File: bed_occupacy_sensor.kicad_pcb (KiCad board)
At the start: 2 copper layers, 10 parts, among them J1 FSR_2, J2 FSR_1, U1 mini_esp32

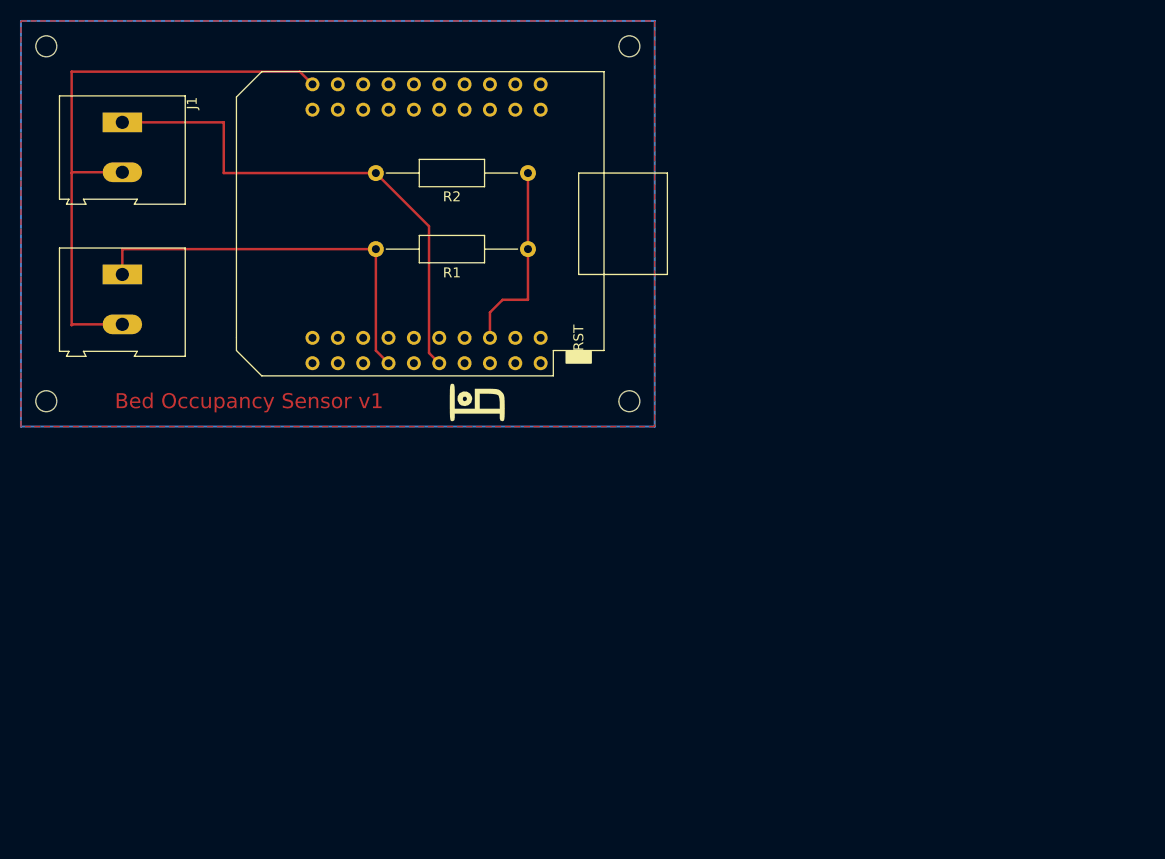
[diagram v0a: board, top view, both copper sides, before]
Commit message: new pcb design all GND connected to ground plane
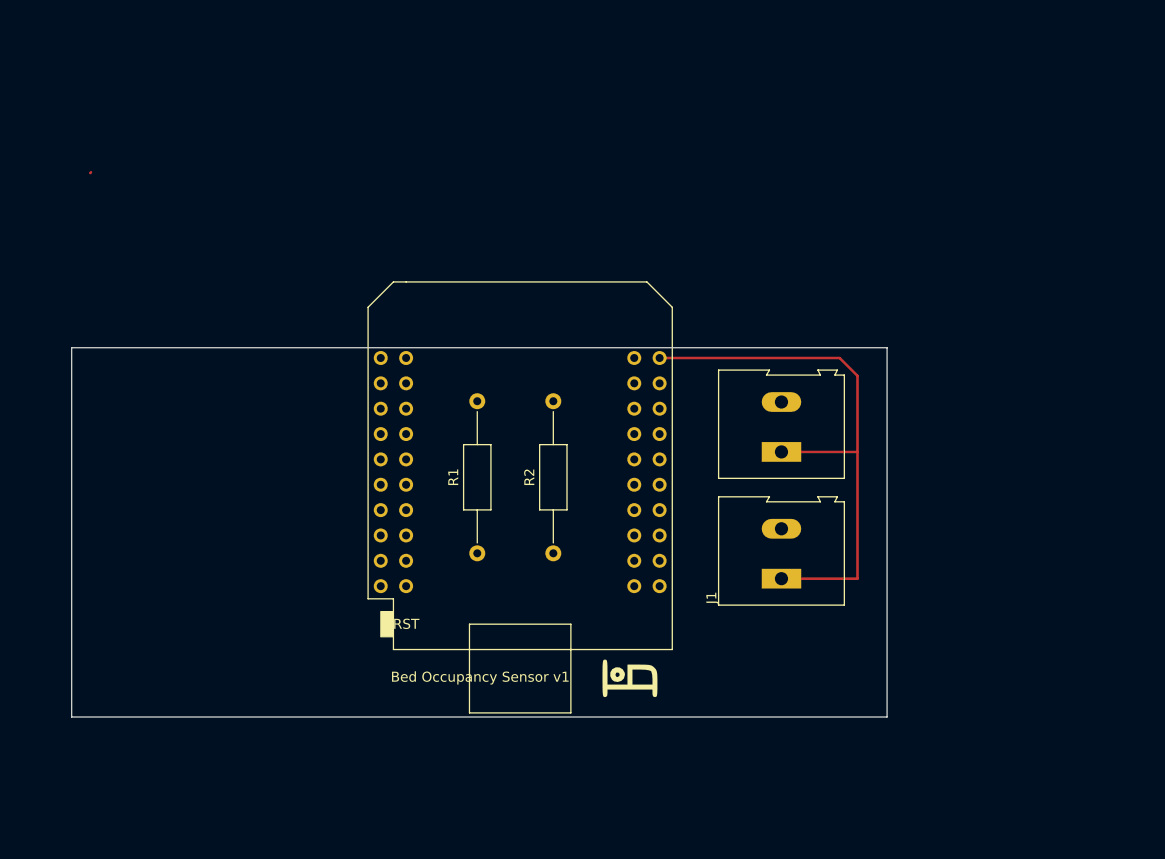
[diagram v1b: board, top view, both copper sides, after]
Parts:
- removed REF** (x4): MountingHole_2.1mm, MountingHole:MountingHole_2.1mm
- moved J1 80.3 mm to (170.2, 104.1), turned to 90 degrees
- moved J2 68.4 mm to (170.2, 91.4), turned to 90 degrees
- moved R2 38.2 mm to (147.3, 101.6), turned to 90 degrees
- moved G*** 31.6 mm to (155.0, 114.0)
- moved R1 30.9 mm to (139.7, 101.6), turned to 90 degrees
- moved U1 26.6 mm to (144.0, 93.5), turned to 0 degrees
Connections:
- J1 pad 1: Net-(J1-Pad1) -> Net-(U1-Pad22)
- J1 pad 2: Net-(U1-Pad22) -> Net-(R1-Pad2)
- J2 pad 1: Net-(J2-Pad1) -> Net-(U1-Pad22)
- J2 pad 2: Net-(U1-Pad22) -> Net-(R2-Pad2)
- R1 pad 2: Net-(J2-Pad1) -> Net-(R1-Pad2)
- R2 pad 2: Net-(J1-Pad1) -> Net-(R2-Pad2)
- U1 pad 11: Net-(J1-Pad1) -> Net-(R2-Pad2)
- U1 pad 7: Net-(J2-Pad1) -> Net-(R1-Pad2)
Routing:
- net Net-(J1-Pad1): track 52.2 -> 0.00 mm
- net Net-(J2-Pad1): track 39.9 -> 0.00 mm
- net Net-(R1-Pad1): track 19.6 -> 0.00 mm
- net Net-(U1-Pad22): track 60.3 -> 56.1 mm
- removed copper zone on F.Cu, net (none)
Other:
- board outline added: 81.7 x 37 mm

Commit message: Save-Changes again
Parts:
- moved R1 46.9 mm to (185.0, 113.6)
- moved R2 46.9 mm to (192.6, 113.6)
- moved U1 46.9 mm to (189.3, 105.5)
- moved G*** 26.0 mm to (165.0, 90.0)
- moved J2 20.4 mm to (164.7, 111.1), turned to -90 degrees
- moved J1 7.96 mm to (164.7, 98.4), turned to -90 degrees
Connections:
- net Net-(R1-Pad1) renamed /+3V3
- net Net-(R1-Pad2) renamed /SIDE_A
- net Net-(R2-Pad2) renamed /SIDE_B
- J1 pad 1: Net-(U1-Pad22) -> /GND
- J2 pad 1: Net-(U1-Pad22) -> /GND
- U1 pad 1: unconnected-(U1-Pad1) -> /GND
- U1 pad 22: Net-(U1-Pad22) -> /GND
- U1 pad 33: unconnected-(U1-Pad33) -> /GND
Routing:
- net /SIDE_B: track 0.00 -> 74.8 mm
- net Net-(U1-Pad22): track 56.1 -> 0.00 mm
- net /SIDE_A: track 0.00 -> 22.4 mm
- net /+3V3: track 0.00 -> 15.5 mm
- added copper zone on F.Cu, net /GND
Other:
- board size 81.7 x 37 mm -> 55 x 45 mm

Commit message: pcb update & smaller pcb, groundplate over complete area, drillholes in gerberfiles included
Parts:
- moved G*** 34.0 mm to (171.8, 123.3)
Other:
- board size 55 x 45 mm -> 48 x 34 mm
- board text added: "ESP32 / D1 mini"
- board text added: "USB-side"
